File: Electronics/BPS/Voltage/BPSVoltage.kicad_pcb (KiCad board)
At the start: 2 copper layers, 65 x 75 mm, 122 parts, among them J1 Conn1, J2 Conn2, J3 Conn_01x06, J4 Conn_01x07, J5 Conn_01x03, J6 Conn_01x05, J7 Conn_02x03_Counter_Clockwise, Q1 BSS308PE, Q10 BSS308PE, Q11 BSS308PE, Q12 BSS308PE, Q13 BSS308PE, Q2 BSS308PE, Q3 BSS308PE, Q4 BSS308PE, Q5 NSV1C201MZ4, Q6 BSS308PE, Q7 BSS308PE, Q8 BSS308PE, Q9 BSS308PE, U1 LTC6811-1, U2 HX1188FNL

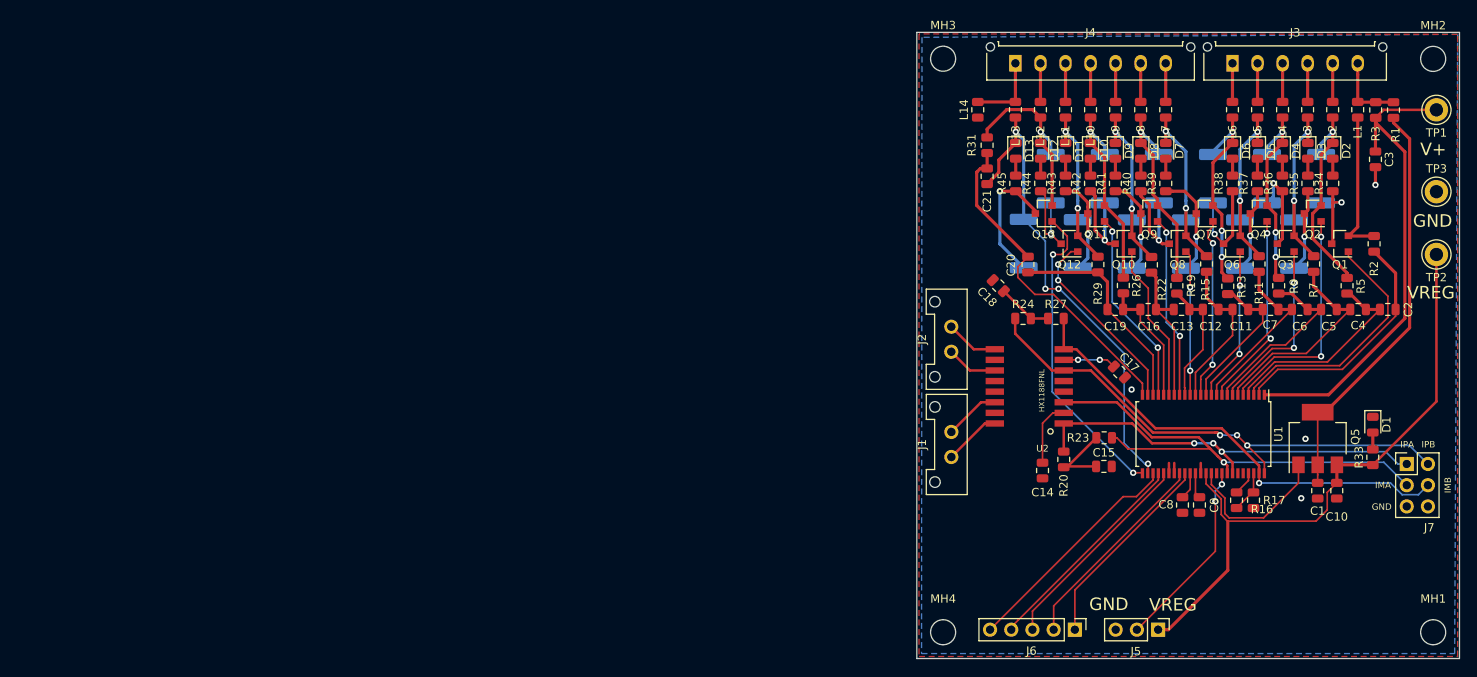
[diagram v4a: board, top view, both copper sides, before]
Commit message: Restructured, spaced out, reduced # of vias
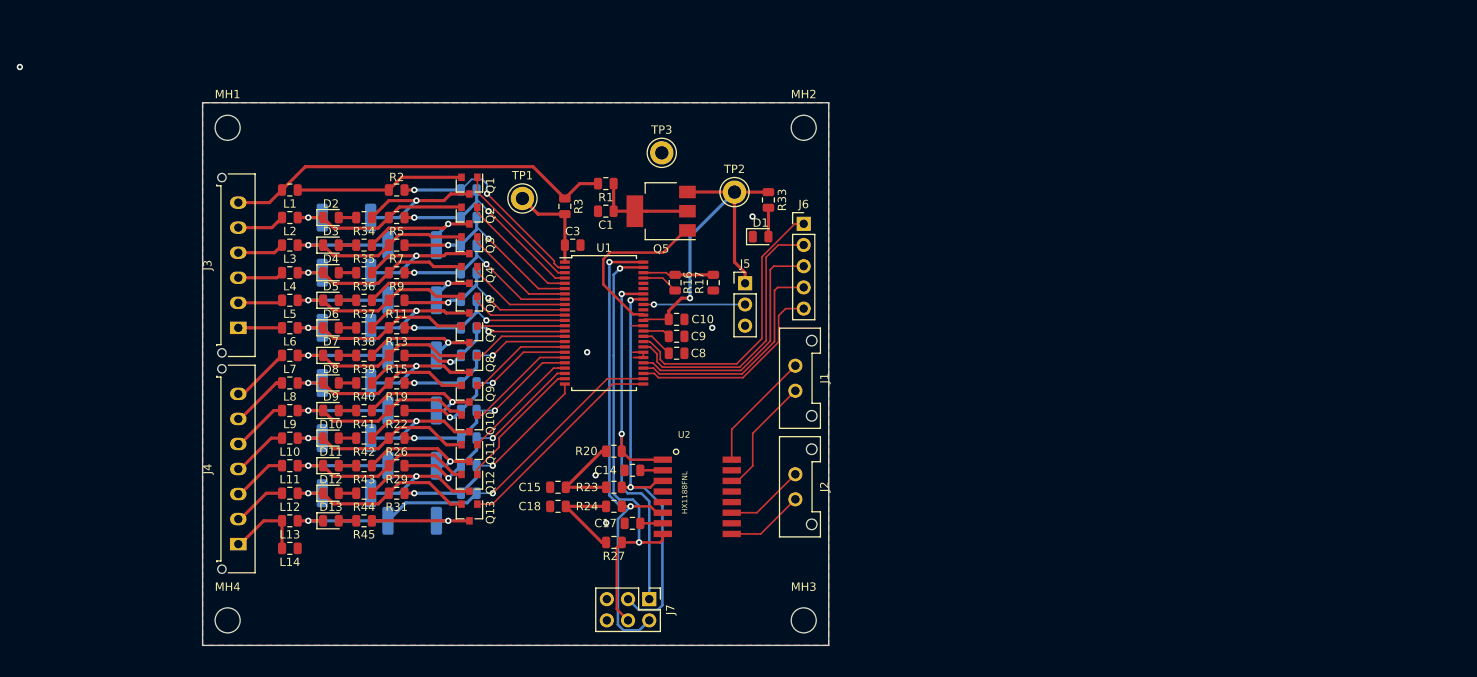
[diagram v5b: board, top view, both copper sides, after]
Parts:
- C11, C12, C13, C16, C19, C2, C20, C21, C4, C5, C6, C7: moved to B.Cu
- moved MH1 156.5 mm to (48.0, 53.0)
- moved L1 128.3 mm to (55.5, 60.5), turned to 180 degrees
- moved L2 125.6 mm to (55.5, 63.8), turned to 180 degrees
- moved J3 123.2 mm to (49.3, 77.0), turned to 90 degrees
- moved L3 123.0 mm to (55.5, 67.1), turned to 180 degrees
- moved L4 120.5 mm to (55.5, 70.4), turned to 180 degrees
- moved D2 120.3 mm to (60.4, 63.8), turned to 0 degrees
- moved L5 118.1 mm to (55.5, 73.7), turned to 180 degrees
- moved D3 117.6 mm to (60.4, 67.1), turned to 0 degrees
- moved R2 117.3 mm to (68.2, 60.5), turned to 180 degrees
- moved R4 116.8 mm to (62.2, 63.8), turned to 0 degrees
- moved R34 116.1 mm to (64.3, 63.8), turned to 180 degrees
- moved L6 115.9 mm to (55.5, 77.0), turned to 180 degrees
- moved D4 114.9 mm to (60.4, 70.4), turned to 0 degrees
- moved R5 114.1 mm to (68.2, 63.8), turned to 180 degrees
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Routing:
- net Net-(C3-Pad1): track 57.8 -> 11.6 mm
- net /V12: track 8.92 -> 47.2 mm
- net Net-(C1-Pad1): track 49.6 -> 12.1 mm
- net /VREG: track 75.1 -> 43.4 mm, vias 0 -> 1
- net Net-(C20-Pad1): track 40.5 -> 26.1 mm, vias 0 -> 2
- net Net-(Q1-Pad1): track 30.2 -> 16.2 mm
- net Net-(Q2-Pad1): track 27.9 -> 14.6 mm, vias 2 -> 0
- net Net-(Q13-Pad1): track 37.4 -> 25.8 mm, vias 2 -> 0
- net Net-(Q7-Pad1): track 21.9 -> 10.5 mm, vias 2 -> 0
- net /ISOMD: track 23.0 -> 12.2 mm, vias 2 -> 1
- net Net-(Q4-Pad1): track 23.5 -> 12.7 mm, vias 2 -> 0
- net /Batt2: track 21.0 -> 31.7 mm, vias 2 -> 1
- net /Batt4: track 21.2 -> 31.5 mm, vias 2 -> 1
- net /Batt6: track 21.4 -> 31.3 mm, vias 2 -> 1
- net Net-(Q9-Pad1): track 21.9 -> 12.4 mm, vias 2 -> 0
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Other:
- board size 65 x 75 mm -> 75 x 65 mm
- board text removed: "GND"
- board text removed: "IMA"
- board text removed: "IMB"
- board text removed: "IPA"
- board text removed: "IPB"
- board text removed: "V+"
- board text removed: "VREG"

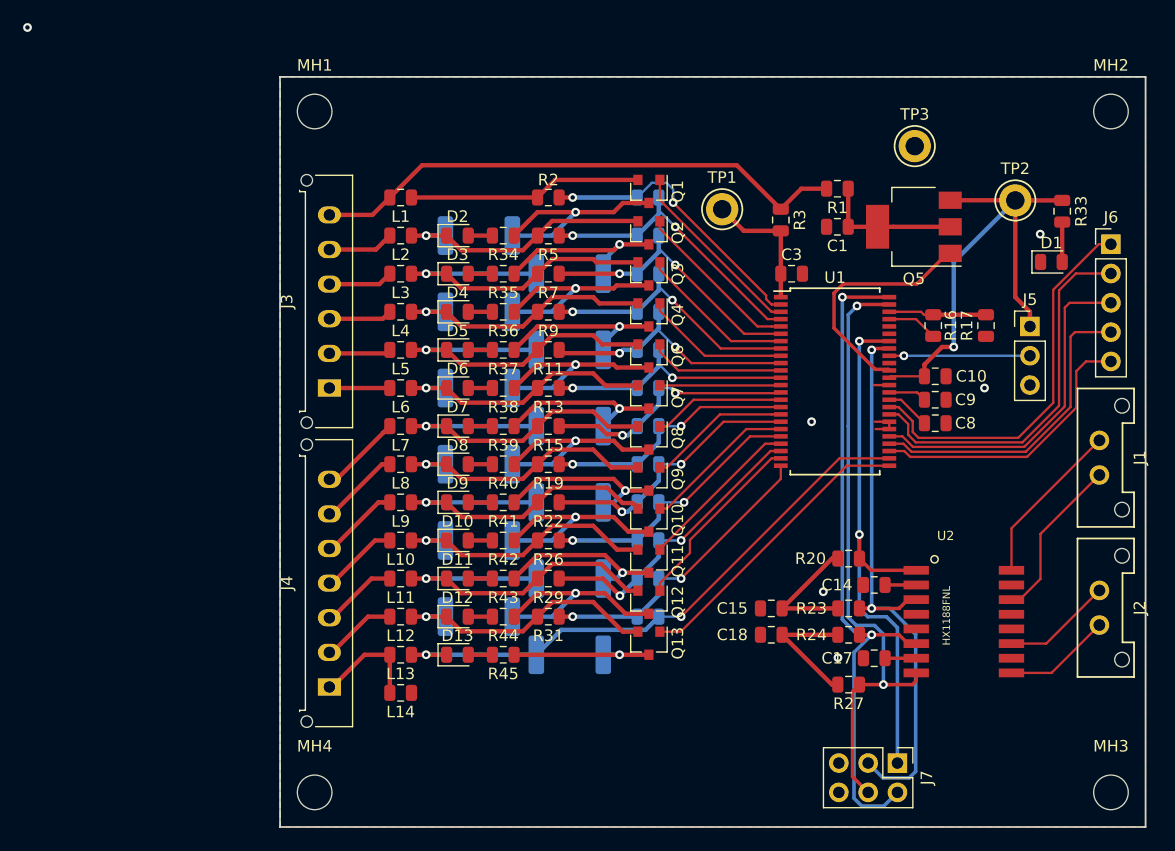
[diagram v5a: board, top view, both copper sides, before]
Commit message: Remodelled the board
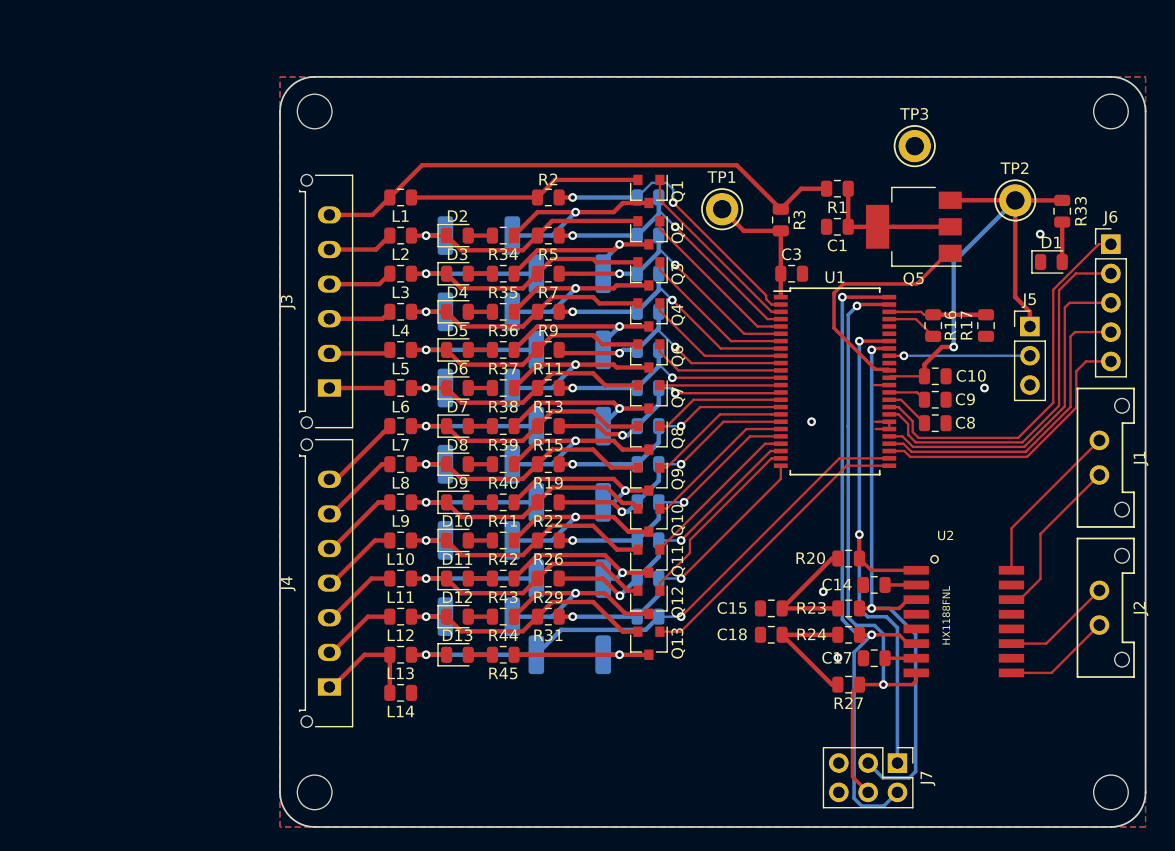
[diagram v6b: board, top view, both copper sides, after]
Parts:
- renumbered MH1 to ?, MH2 to ?, MH3 to ?, MH4 to ?
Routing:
- net (no net): vias 1 -> 0
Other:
- outline, holes or cut-outs redrawn
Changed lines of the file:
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@@
   (general
     (thickness 1.6)
-    (drawings 6)
-    (tracks 630)
+    (drawings 8)
+    (tracks 629)
     (zones 0)
     (modules 122)
@@
   )
   (setup
-    (last_trace_width 0.381)
+    (last_trace_width 0.25)
     (user_trace_width 0.2032)
     (user_trace_width 0.254)
@@
     (tags "mounting hole 3mm no annular")
     (attr virtual)
-    (fp_text reference MH1 (at 0 -4) (layer F.SilkS)
+    (fp_text reference "" (at 0 -4) (layer F.SilkS)
       (effects (font (size 1 1) (thickness 0.15)))
     )
@@
     (tags "mounting hole 3mm no annular")
     (attr virtual)
-    (fp_text reference MH2 (at 0 -4) (layer F.SilkS)
+    (fp_text reference "" (at 0 -4) (layer F.SilkS)
       (effects (font (size 1 1) (thickness 0.15)))
     )
@@
     (tags "mounting hole 3mm no annular")
     (attr virtual)
-    (fp_text reference MH3 (at 0 -4) (layer F.SilkS)
+    (fp_text reference "" (at 0 -4) (layer F.SilkS)
       (effects (font (size 1 1) (thickness 0.15)))
     )
@@
     (tags "mounting hole 3mm no annular")
     (attr virtual)
-    (fp_text reference MH4 (at 0 -4) (layer F.SilkS)
+    (fp_text reference "" (at 0 -4) (layer F.SilkS)
       (effects (font (size 1 1) (thickness 0.15)))
     )
@@
       (net 16 "Net-(C14-Pad1)"))
   )
-  (gr_line (start 45 50) (end 120 50) (layer Edge.Cuts) (width 0.15))
-  (gr_line (start 45 115) (end 45 50) (layer Edge.Cuts) (width 0.15))
-  (gr_line (start 120 115) (end 45 115) (layer Edge.Cuts) (width 0.15))
-  (gr_line (start 120 50) (end 120 115) (layer Edge.Cuts) (width 0.15))
-  (dimension 65 (width 0.3) (layer F.SilkS)
-    (gr_text "65.000 mm" (at 137.1 82.5 270) (layer F.SilkS)
-      (effects (font (size 1.5 1.5) (thickness 0.3)))
-    )
-    (feature1 (pts (xy 120 115) (xy 135.586421 115)))
-    (feature2 (pts (xy 120 50) (xy 135.586421 50)))
-    (crossbar (pts (xy 135 50) (xy 135 115)))
-    (arrow1a (pts (xy 135 115) (xy 134.413579 113.873496)))
-    (arrow1b (pts (xy 135 115) (xy 135.586421 113.873496)))
-    (arrow2a (pts (xy 135 50) (xy 134.413579 51.126504)))
-    (arrow2b (pts (xy 135 50) (xy 135.586421 51.126504)))
-  )
-  (dimension 75 (width 0.3) (layer F.SilkS)
-    (gr_text "75.000 mm" (at 82.5 37.9) (layer F.SilkS)
-      (effects (font (size 1.5 1.5) (thickness 0.3)))
-    )
-    (feature1 (pts (xy 120 50) (xy 120 39.413579)))
-    (feature2 (pts (xy 45 50) (xy 45 39.413579)))
-    (crossbar (pts (xy 45 40) (xy 120 40)))
-    (arrow1a (pts (xy 120 40) (xy 118.873496 40.586421)))
-    (arrow1b (pts (xy 120 40) (xy 118.873496 39.413579)))
-    (arrow2a (pts (xy 45 40) (xy 46.126504 40.586421)))
-    (arrow2b (pts (xy 45 40) (xy 46.126504 39.413579)))
-  )
-  (via (at 23.114 45.72) (size 0.762) (drill 0.381) (layers F.Cu B.Cu) (net 0))
+  (gr_line (start 45 53) (end 45 112) (layer Edge.Cuts) (width 0.15))
+  (gr_line (start 117 50) (end 48 50) (layer Edge.Cuts) (width 0.15))
+  (gr_line (start 120 112) (end 120 53) (layer Edge.Cuts) (width 0.15))
+  (gr_line (start 48 115) (end 117 115) (layer Edge.Cuts) (width 0.15))
+  (gr_arc (start 48 112) (end 45 112) (angle -90) (layer Edge.Cuts) (width 0.15))
+  (gr_arc (start 48 53) (end 48 50) (angle -90) (layer Edge.Cuts) (width 0.15))
+  (gr_arc (start 117 53) (end 120 53) (angle -90) (layer Edge.Cuts) (width 0.15))
+  (gr_arc (start 117 112) (end 117 115) (angle -90) (layer Edge.Cuts) (width 0.15))
   (segment (start 94.234 62.992) (end 96.774 62.992) (width 0.381) (layer F.Cu) (net 1))
   (segment (start 98.155 62.992) (end 103.074 62.992) (width 0.381) (layer F.Cu) (net 1))

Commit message: Footprints, BOM, and final board edits.
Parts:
- J3: footprint Connector_Molex:Molex_Micro-Fit_3.0_43650-0615_1x06_P3.00mm_Vertical -> UTSVT_Connectors:Molex_MicroFit_01x06_Horizontal
- J4: footprint Connector_Molex:Molex_Micro-Fit_3.0_43650-0715_1x07_P3.00mm_Vertical -> UTSVT_Connectors:Molex_MicroFit_01x07_Horizontal
- J7: value Conn_02x03_Counter_Clockwise -> Conn_01x05; footprint Connector_PinHeader_2.54mm:PinHeader_2x03_P2.54mm_Vertical -> Connector_PinHeader_2.54mm:PinHeader_1x05_P2.54mm_Vertical
- moved J6 10.2 mm to (117.0, 74.7), turned to 180 degrees
- moved J4 9.41 mm to (52.0, 93.9), turned to 270 degrees
- moved J3 7.99 mm to (52.0, 69.5), turned to 270 degrees
- moved J7 2.99 mm to (100.1, 112.0)
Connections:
- J6 pad 1: /GPIO5 -> /GPIO1
- J6 pad 2: /GPIO4 -> /GPIO2
- J6 pad 4: /GPIO2 -> /GPIO4
- J6 pad 5: /GPIO1 -> /GPIO5
- J7 pad 2: /IPB -> /IMA
- J7 pad 3: /IMA -> /SDI
- J7 pad 4: /IMB -> /SDO
- U1 pad 43: (no net) -> /SDI
- U1 pad 44: (no net) -> /SDO
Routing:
- net /SDO: track 0.00 -> 46.5 mm, vias 0 -> 1
- net /SDI: track 0.00 -> 44.2 mm, vias 0 -> 2
- net /IPB: track 59.7 -> 39.3 mm
- net /IMB: track 54.1 -> 43.0 mm
- net /IMA: track 50.7 -> 46.4 mm
- net Net-(J4-Pad1): track 9.70 -> 5.99 mm
- net /IPA: track 48.9 -> 52.5 mm, vias 2 -> 3
- net /V12: track 47.2 -> 44.4 mm
- net Net-(J3-Pad2): track 5.36 -> 2.61 mm
- net Net-(J3-Pad1): track 5.24 -> 2.48 mm
- net Net-(J3-Pad5): track 5.74 -> 2.98 mm
- net Net-(J3-Pad4): track 5.61 -> 2.86 mm
- net Net-(J3-Pad3): track 5.49 -> 2.73 mm
- net Net-(J4-Pad2): track 6.52 -> 4.13 mm
- net Net-(J4-Pad3): track 6.64 -> 4.43 mm
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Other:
- rule trace_min: 0.2 -> 0.1524
- board text added: "+"
- board text added: "+V"
- board text added: "-"
- board text added: "0"
- board text added: "1"
- board text added: "12"
- board text added: "2"
- board text added: "3"
- board text added: "4"
- board text added: "5"
- board text added: "COM"
- board text added: "CSB"
- board text added: "GND"
- board text added: "GPIO"
- board text added: "IMA"
- board text added: "IMB"
- board text added: "IN"
- board text added: "IPA"
- board text added: "IPB"
- board text added: "MISO"
- board text added: "MOSI"
- board text added: "OUT"
- board text added: "SCK"
- board text added: "Spring 2019: Monolo Alvarez Chase Block Corbin Capo Richard Li Garrett Wong Sijin Woo"
- board text added: "UTSVT - BPS Voltage v1.0 Spring 2019 Chase Block"
- board text added: "VREG"

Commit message: Logos etc.
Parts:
- added G***: LOGO, UTSVT_Special:UTSVT_Logo_Symbol, F.Cu at (77.2, 110.2)
- added G***: LOGO, UTSVT_Special:Hallock_Image, B.Cu at (100.1, 84.5)
- moved J4 1.51 mm to (52.2, 92.4)
- moved J3 0.63 mm to (52.2, 68.9)
- moved L1 0.44 mm to (55.9, 60.5)
- moved L10 0.44 mm to (55.9, 90.2)
- moved L11 0.44 mm to (55.9, 93.5)
- moved L12 0.44 mm to (55.9, 96.8)
- moved L13 0.44 mm to (55.9, 100.1)
- moved L14 0.44 mm to (55.9, 103.4)
- moved L2 0.44 mm to (55.9, 63.8)
- moved L3 0.44 mm to (55.9, 67.1)
- moved L4 0.44 mm to (55.9, 70.4)
- moved L5 0.44 mm to (55.9, 73.7)
- moved L6 0.44 mm to (55.9, 77.0)
- moved L7 0.44 mm to (55.9, 80.3)
- moved L8 0.44 mm to (55.9, 83.6)
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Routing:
- net GND: track 4.43 -> 22.4 mm, vias 17 -> 19
- net Net-(J4-Pad7): track 5.64 -> 4.25 mm
- net Net-(J4-Pad6): track 5.34 -> 3.95 mm
- net Net-(J4-Pad5): track 5.03 -> 3.80 mm
- net /L10: track 15.9 -> 17.0 mm
- net Net-(J4-Pad4): track 4.73 -> 3.67 mm
- net Net-(J4-Pad3): track 4.43 -> 3.55 mm
- net /Batt8: track 31.1 -> 30.3 mm
- net /Batt6: track 31.3 -> 30.5 mm
- net /Batt5: track 23.5 -> 22.8 mm
- net /Batt4: track 31.5 -> 30.7 mm
- net /Batt3: track 23.7 -> 23.0 mm
- net /Batt2: track 31.7 -> 30.9 mm
- net /Batt11: track 22.9 -> 22.1 mm
- net /Batt10: track 30.9 -> 30.1 mm
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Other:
- board text added: "Spring 2019: Monolo Alvarez Chase Block Corbin Capo Richard Li Austin Tsao Garrett Wong Sihyung Woo Sijin Woo"
- board text removed: "Spring 2019: Monolo Alvarez Chase Block Corbin Capo Richard Li Garrett Wong Sijin Woo"
